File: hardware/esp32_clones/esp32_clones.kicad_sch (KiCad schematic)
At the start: 31 parts, among them J1 Barrel_Jack, J2 Micro_SD_Card, J3 AudioJack2_Ground, J6 USB_A, J7 USB_A, J8 USB_A, J9 DA15_Pins

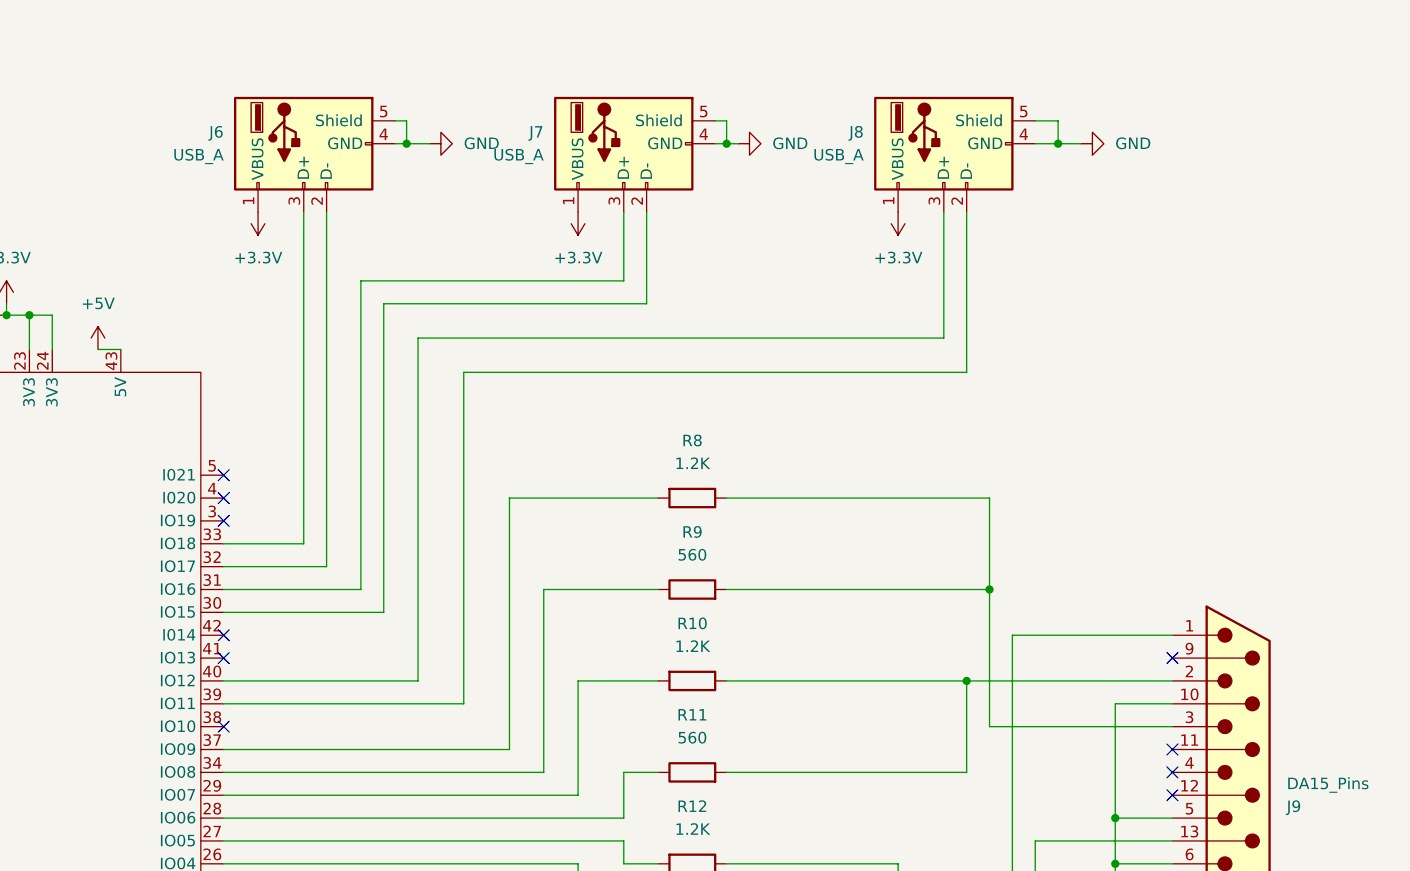
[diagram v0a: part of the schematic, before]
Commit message: - Drove the audio output in stereo, with the left channel on GPIO47 and the right channel on GPIO48. The CP400 sound source is mono, so both channels carry the same signal. - Raised the audio carrier well above the audible range, so the board's audio filter now removes almost all of it instead of leaving an ultrasonic tone on the jack.
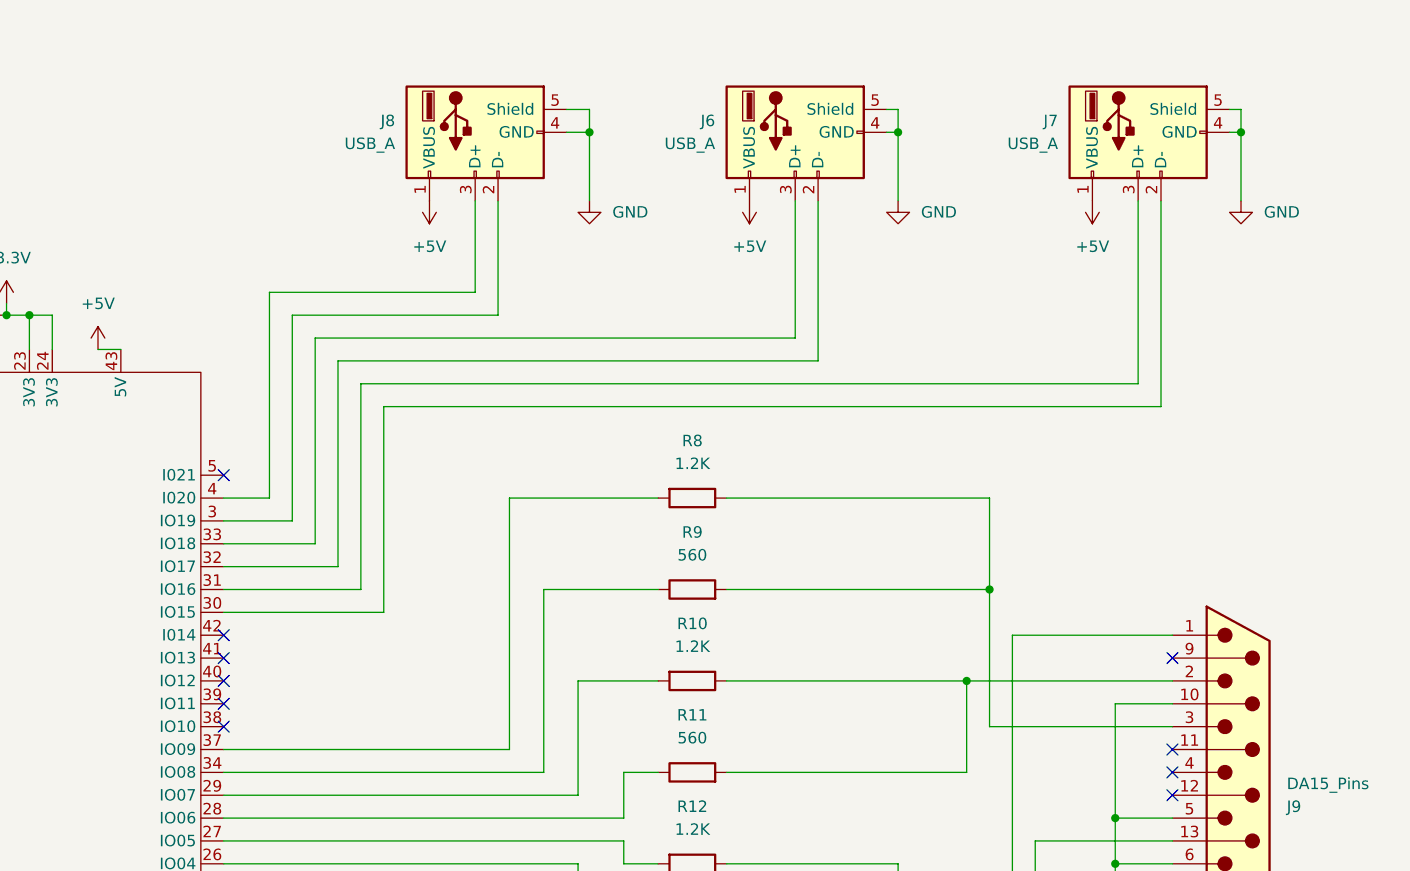
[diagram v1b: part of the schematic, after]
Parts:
- C2, C3: footprint Capacitor_SMD:CP_Elec_6.3x3 -> Capacitor_SMD:CP_Elec_5x4.5
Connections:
- net +3.3V: no longer J6.1 (VBUS), J7.1 (VBUS), J8.1 (VBUS)
- net +5V: now also J6.1 (VBUS), J7.1 (VBUS), J8.1 (VBUS)
- net at U1.3 (IO19): now also J8.2 (D-)
- net at U1.39 (IO11): no longer J8.2 (D-)
- net at U1.4 (I020): now also J8.3 (D+)
- net at U1.40 (IO12): no longer J8.3 (D+)
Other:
- moved on the sheet: J6, J7, J8

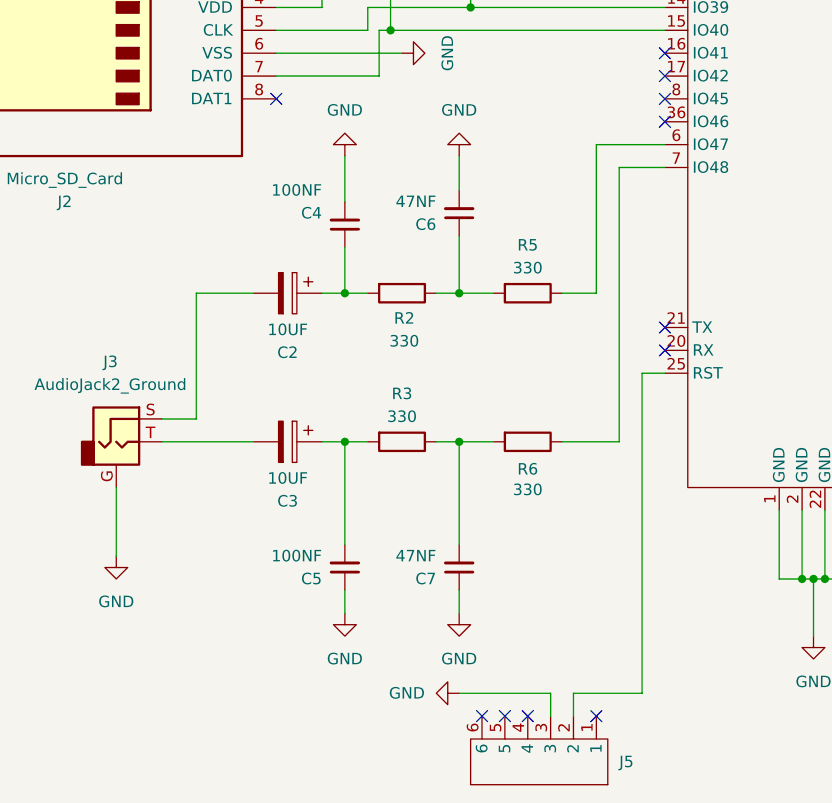
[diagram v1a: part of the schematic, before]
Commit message: - New board and small adjustments for sound on CP400 emulator
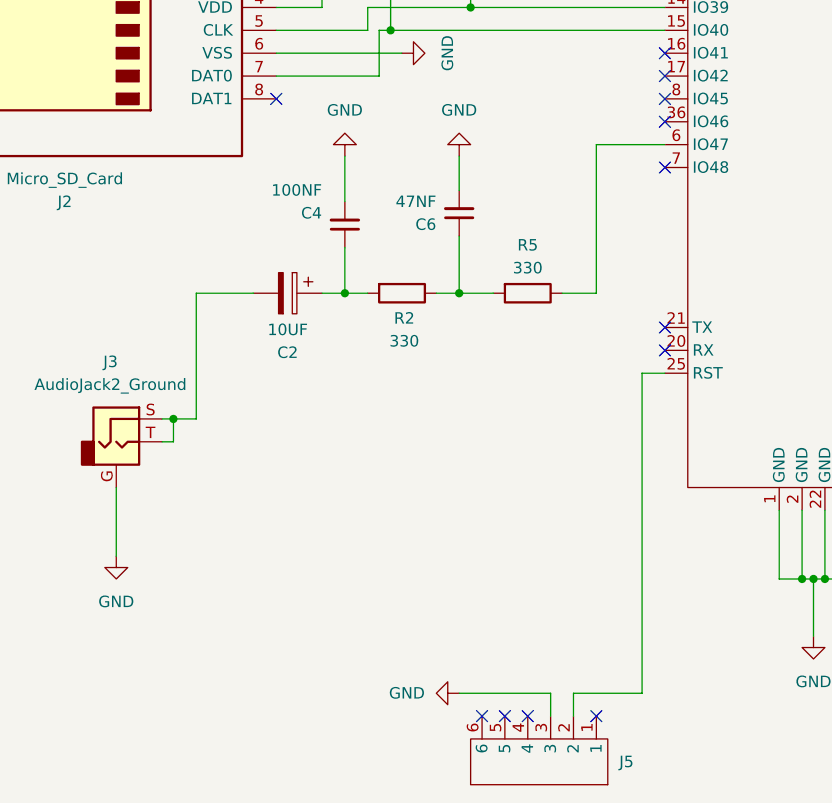
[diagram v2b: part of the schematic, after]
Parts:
- removed C3: 10UF, Capacitor_SMD:CP_Elec_5x4.5, symbol Device:C_Polarized
- removed C5: 100NF, Capacitor_SMD:C_0805_2012Metric_Pad1.18x1.45mm_HandSolder, symbol Device:C_Small
- removed C7: 47NF, Capacitor_SMD:C_0805_2012Metric_Pad1.18x1.45mm_HandSolder, symbol Device:C_Small
- removed R3, R6: 330, Resistor_SMD:R_0805_2012Metric_Pad1.20x1.40mm_HandSolder, symbol Device:R
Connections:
- net at J3.T: now also C2.2, J3.S
- no-connect marks 32 -> 33
